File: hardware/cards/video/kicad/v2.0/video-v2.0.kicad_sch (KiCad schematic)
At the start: 108 parts, among them IC1 74ALS08, IC15 IDT7134, IC17 MC6845, IC18 74S85, IC19 74LS00, IC20 74LS04, IC21 74LS90, IC22 74LS175, IC23 74LS174, IC24 74LS166, IC25 2732, IC26 74LS86, IC27 7416, IC28 74LS163, IC30 74LS138, IC31 74LS32, IC32 74LS32, IC33 74LS273, IC34 74LS244, IC35 74LS157, IC36 74LS157, IC37 74LS157, IC38 74LS157, IC39 62256, IC40 74LS244, IC41 74LS374, IC42 74LS374, IC43 74LS166, IC44 74LS74, IC45 74LS20, IC46 74LS04, IC47 74LS08, IC48 74LS10, IC49 ATmega328P-P, IC50 74LS374, IC51 74LS374, IC52 74LS244, IC53 74LS74, J1 RCA, J2 KEYBOARD, J3 MOUSE, J4 FTDI, Q2 12MHz, X1 DIN41612 96, X2 DB9 F, Y1 16MHz

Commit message: feat(video): V2.0 review fixes and two features, board rebuilt
The design review's HIGH and MED fixes in the circuit: V2-1 BUSY/SRC swapped on the ATmega (pins 17/19), V2-2 the
Mini-DIN footprint drawn from the Same Sky MD-60SM data sheet, V2-4 the muxes' select from QC OR RCO, V2-5 IC40 enabled
by -WE, V2-6 MRST through IC27/E,F (D1 gone), V2-7/8 -INT = INTREQ AND FULL (new IC54 74HCT08) with pull-ups on LDDATA
and RDCMD, V2-9/12 HCT parts, V2-10 an AT28C64B-15 character generator; LOW V2-16/17/20/21 (decoupling, PTC, J4
legend, BOM.md).

Direct mode: with GFX-ON = 0 the CPU owns the graphics RAM (NMUX = NAND(QC OR RCO, GFX-ON) holds the CPU address,
-WE = NOT GWR, -OE from the window read, reads through the new bypass buffer IC55 74HCT244, GD pull-ups RN3).
Text-only build: R25/R26 pull-down pads on GDOT and WRQ, IN PC bit 3 = TEXT-ONLY (IC44/B, R27);
text_only_check() proves those are the only nets the left-off parts drive.

build.sh: order 3 complete, 308 vias, DRC 0 unconnected / no copper findings, netlist proof 215/215, ERC off-grid only,
verify PASS (173 key connections). Not to be ordered before the re-review.

Co-Authored-By: Claude Opus 5.5 <noreply@anthropic.com>
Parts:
- removed D1: 1N4148, Diode_THT:D_DO-35_SOD27_P7.62mm_Horizontal, symbol Device:D
- added C58, C59: 100n, Capacitor_THT:C_Disc_D5.0mm_W2.5mm_P2.50mm, symbol Device:C
- added F1: 0.5A PTC, Fuse:Fuse_Bourns_MF-RHT050, symbol Device:Polyfuse
- added IC54: 74HCT08, Package_DIP:DIP-14_W7.62mm, symbol 74xx:74LS08
- added IC55: 74HCT244, Package_DIP:DIP-20_W7.62mm, symbol 74xx:74LS244
- added R21: 4.7k, Resistor_THT:R_Axial_DIN0207_L6.3mm_D2.5mm_P7.62mm_Horizontal, symbol Device:R
- added R22, R23, R24, R27: 10k, Resistor_THT:R_Axial_DIN0207_L6.3mm_D2.5mm_P7.62mm_Horizontal, symbol Device:R
- added R25, R26: 1k, Resistor_THT:R_Axial_DIN0207_L6.3mm_D2.5mm_P7.62mm_Horizontal, symbol Device:R
- added RN3: 10k x8, Resistor_THT:R_Array_SIP9, symbol Device:R_Network08
- C16: value 10u -> 47u; footprint Capacitor_THT:CP_Radial_D5.0mm_P2.50mm -> Capacitor_THT:CP_Radial_D6.3mm_P2.50mm
- IC25: value 2732 -> AT28C64B-15; footprint Package_DIP:DIP-24_W15.24mm -> Package_DIP:DIP-28_W15.24mm; symbol video-v2.0-local:2732 -> Memory_EEPROM:KM28C64A
- IC33: value 74LS273 -> 74HCT273
- IC40: value 74LS244 -> 74HCT244
- IC41, IC51: value 74LS374 -> 74HCT374
- IC53: value 74LS74 -> 74HCT74
- J2, J3: footprint video-v2.0-local:MiniDIN6_PS2 -> video-v2.0-local:MiniDIN6_MD-60SM
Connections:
- net -RESET: now also IC27.11
- net ADDR0: now also IC35.3 (I1a); no longer IC35.2 (I0a)
- net ADDR1: now also IC35.6 (I1b); no longer IC35.5 (I0b)
- net ADDR10: now also IC37.10 (I1c); no longer IC37.11 (I0c)
- net ADDR2: now also IC35.10 (I1c); no longer IC35.11 (I0c)
- net ADDR3: now also IC35.13 (I1d); no longer IC35.14 (I0d)
- net ADDR4: now also IC36.3 (I1a); no longer IC36.2 (I0a)
- net ADDR5: now also IC36.6 (I1b); no longer IC36.5 (I0b)
- net ADDR6: now also IC36.10 (I1c); no longer IC36.11 (I0c)
- net ADDR7: now also IC36.13 (I1d); no longer IC36.14 (I0d)
- net ADDR8: now also IC37.3 (I1a); no longer IC37.2 (I0a)
- net ADDR9: now also IC37.6 (I1b); no longer IC37.5 (I0b)
- net BUSY: now also IC49.17 (PB3); no longer IC49.19 (PB5)
- net CA3: now also IC25.7 (A3); no longer IC25.5 (A3)
- net CA4: now also IC25.6 (A4); no longer IC25.4 (A4)
- net CA5: now also IC25.5 (A5); no longer IC25.3 (A5)
- net CA6: now also IC25.4 (A6); no longer IC25.2 (A6)
- net CA7: now also IC25.3 (A7); no longer IC25.1 (A7)
- net CA8: now also IC25.25 (A8); no longer IC25.23 (A8)
- net CG0: now also IC25.11 (I/O0); no longer IC25.9 (O0)
- net CG1: now also IC25.12 (I/O1); no longer IC25.10 (O1)
- net CG2: now also IC25.13 (I/O2); no longer IC25.11 (O2)
- net CG3: now also IC25.15 (I/O3); no longer IC25.13 (O3)
- net CG4: now also IC25.16 (I/O4); no longer IC25.14 (O4)
- net CG5: now also IC25.17 (I/O5); no longer IC25.15 (O5)
- net CG6: now also IC25.18 (I/O6); no longer IC25.16 (O6)
- net CG7: now also IC25.19 (I/O7); no longer IC25.17 (O7)
- net CPAGE: now also IC38.10 (I1c); no longer IC38.11 (I0c)
- net CRTCCLOCK: now also IC32.9; no longer IC35.1 (S), IC36.1 (S), IC37.1 (S), IC38.1 (S), IC46.1
- net DATA0: now also IC55.18 (O0a)
- net DATA1: now also IC55.16 (O1a)
- net DATA2: now also IC55.14 (O2a)
- net DATA3: now also IC55.12 (O3a)
- net DATA4: now also IC55.9 (O0b)
- net DATA5: now also IC55.7 (O1b)
- net DATA6: now also IC55.5 (O2b)
- net DATA7: now also IC55.3 (O3b)
- net DOTS: now also IC25.21 (A10); no longer IC25.19 (A10)
- net DPAGE: now also IC38.11 (I0c); no longer IC38.10 (I1c)
- net FULL: now also IC54.5
- net GD0: now also IC55.2 (I0a), RN3.2 (R1)
- net GD1: now also IC55.4 (I1a), RN3.3 (R2)
- net GD2: now also IC55.6 (I2a), RN3.4 (R3)
- net GD3: now also IC55.8 (I3a), RN3.5 (R4)
- net GD4: now also IC55.11 (I0b), RN3.6 (R5)
- net GD5: now also IC55.13 (I1b), RN3.7 (R6)
- net GD6: now also IC55.15 (I2b), RN3.8 (R7)
- net GD7: now also IC55.17 (I3b), RN3.9 (R8)
- net GDOT: now also R25.1
- net GFXON: now also IC19.13, IC44.4 (~{S}), IC46.1, IC48.11
- net GND: now also IC25.14 (GND), IC25.2 (A12), IC25.23 (A11), IC25.24 (A9), IC44.13 (~{R}), IC46.13, C58.2, C59.2, IC54.10, IC54.12, IC54.13, IC54.7 (GND), IC54.9, IC55.10 (GND), R24.2, R25.2, R26.2; no longer IC25.12 (GND), IC25.18 (~{CE}), IC25.21 (A11), IC27.11, IC27.13, IC32.10, IC32.12, IC32.13, IC32.9, IC34.8 (I3a)
- net GRDOE: now also IC54.2; no longer IC41.1 (OE)
- net GSEL: now also IC45.9, IC48.9
- net GWE: now also IC40.1 (OEa), IC40.19 (OEb)
- net INTREQ: now also IC54.4, R24.1; no longer IC27.9
- net LDDATA: now also R22.1
- net MEMRD: now also IC45.10, IC48.10
- net MRST: now also IC27.12
- net PLANE0: now also IC37.13 (I1d); no longer IC37.14 (I0d)
- net PLANE1: now also IC38.3 (I1a); no longer IC38.2 (I0a)
- net PLANE2: now also IC38.6 (I1b); no longer IC38.5 (I0b)
- net RCO: now also IC32.10
- net RDCMD: now also R23.1
- net SRC: now also IC49.19 (PB5); no longer IC49.17 (PB3)
- net VADDR0: now also IC35.2 (I0a); no longer IC35.3 (I1a)
- net VADDR1: now also IC35.5 (I0b); no longer IC35.6 (I1b)
- net VADDR10: now also IC37.11 (I0c); no longer IC37.10 (I1c)
- net VADDR2: now also IC35.11 (I0c); no longer IC35.10 (I1c)
- net VADDR3: now also IC35.14 (I0d); no longer IC35.13 (I1d)
- net VADDR4: now also IC36.2 (I0a); no longer IC36.3 (I1a)
- net VADDR5: now also IC36.5 (I0b); no longer IC36.6 (I1b)
- net VADDR6: now also IC36.11 (I0c); no longer IC36.10 (I1c)
- net VADDR7: now also IC36.14 (I0d); no longer IC36.13 (I1d)
- net VADDR8: now also IC37.2 (I0a); no longer IC37.3 (I1a)
- net VADDR9: now also IC37.5 (I0b); no longer IC37.6 (I1b)
- net VCC: now also IC25.27 (~{WE}), IC25.28 (VCC), C58.1, C59.1, F1.1, IC54.14 (VCC), IC55.20 (VCC), R21.2, R22.2, R23.2, R27.2, RN3.1 (common); no longer IC19.12, IC19.13, IC25.24 (VCC), IC44.13 (~{R}), IC44.4 (~{S}), IC45.10, IC45.12, IC45.9, IC48.10, IC48.11, IC48.9, J2.4 (+5V), J3.4 (+5V)
- net VROWS0: now also IC25.10 (A0), IC37.14 (I0d); no longer IC25.8 (A0), IC37.13 (I1d)
- net VROWS1: now also IC25.9 (A1), IC38.2 (I0a); no longer IC25.7 (A1), IC38.3 (I1a)
- net VROWS2: now also IC25.8 (A2), IC38.5 (I0b); no longer IC25.6 (A2), IC38.6 (I1b)
- net WEPH: now also IC32.12; no longer IC45.4
- net WRQ: now also R26.1
- net WSLOT: no longer IC46.13
- net WEPH2: now reaches IC32.11
- net WEPH2: now also IC45.4
- net SRDOE: now reaches IC48.8
- net SRDOE: now also IC41.1 (OE)
- net TXTONLY: now reaches IC44.9 (Q)
- net TXTONLY: now also IC34.8 (I3a), R27.1
- net QCR: now reaches IC32.8
- net QCR: now also IC19.12
- net RESETH: now reaches IC27.10
- net RESETH: now also IC27.13, R21.1
- net DRDOE: now reaches IC45.8
- net DRDOE: now also IC55.1 (OEa), IC55.19 (OEb)
- net NMUX: now reaches IC19.11
- net NMUX: now also IC35.1 (S), IC36.1 (S), IC37.1 (S), IC38.1 (S), IC45.2, IC54.1
- removed net -WSLOT: IC40.1 (OEa), IC40.19 (OEb), IC46.12
- removed net NQC: IC1.5, IC45.2, IC46.2
- new net INTG: IC27.9, IC54.6
- new net NGFX: IC32.13, IC45.12, IC46.2
- new net OEY: IC1.5, IC54.3
- new net PS2VCC: F1.2, J2.4 (+5V), J3.4 (+5V)
- no-connect marks 91 -> 88
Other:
- note added: "GRAPHICS RAM $D800-$DFFF: SLOT LOGIC (GFX-ON = 1) / DIRECT MODE (GFX-ON = 0)"
- note removed: "GRAPHICS RAM $D800-$DFFF: SLOT LOGIC (QC: CPU / DISPLAY HALF)"
- moved on the sheet: C16, C17, C18, C19, C20, C21, C22, C23, C24, C25, C26, C27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

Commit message: fix(video): V2.0 rebuilt for the re-review - R2-1 Mini-DIN side-leg slots 1.2 x 2.6, R2-2 IC55 up 0.6 mm, R2-3 -RESET buffered by IC54/C
R2-1: MD-60SM side-leg slots 2.6 x 1.2 mm plated, pads 3.3 x 1.9, same centres (the 0.54 mm legs now 0.21 mm inside
the outer wall, 0.45 inside the inner; earth slot unchanged). R2-2: IC55 at (156.0, 78.7): 3.30 mm from IC19/IC1's end
pins, 3.22 from IC42's (a socket needs <= 3.2). R2-3: IC27/E's input is RESETB = IC54/C (74HCT08, -RESET AND VCC: a
buffer, same sense), so the bus -RESET sees one HCT input. R2-14: verify's KEY +16 nets (MEMWR path, IC44.1, IC53/A,
IC40 A/Y, the jacks' shields), check() fails on a left-off IC without an OUTPUTS entry.
Routed anew: order 6 (orders 3, 4, 17, 0, 1, 2, 5, 7 tried; 5 also clean): 0 unrouted, 328 vias. Netlist proof MATCH
216/216, DRC 0 unconnected / no copper findings / parity 0, ERC off-grid only, verify PASS (189).

Co-Authored-By: Claude Opus 5.5 <noreply@anthropic.com>
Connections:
- net -RESET: now also IC54.9; no longer IC27.11
- net GND: no longer IC54.10, IC54.9
- net VCC: now also IC54.10
- net RESETB: now reaches IC54.8
- net RESETB: now also IC27.11
- no-connect marks 88 -> 87
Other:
- moved on the sheet: IC54C, IC54D

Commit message: fix(video): V2.0 rebuilt for the rest of the re-review - socket-outline check (R2-2), the 6845's B grade and C16 16 V (R2-7), the silkscreen placed clear (R2-9)
R2-2: gen_v20.py place now checks every DIP socket's outline (pin rows + 1.3 mm at the sides, end pins + 1.9 mm at
the ends: the widest stamped sockets) against every other socket and every part's pads and body, over the whole
board (socket_check). It found RN3 and C59 meeting IC55's end wall: both 0.3 mm left. PASS, the closest IC42 / IC55
0.02 mm, IC19 / IC1 / IC55 0.10.
R2-7: IC17's value HD68B45SP / MC68B45P (the 2 MHz bus grade; Hitachi's letters to verify on the part), C16 47u 16V;
BUY notes for IC39 (-55 recommended, R2-8), IC41 / IC55 (74ACT fallback, R2-6), C16; BOM.md regenerated.
R2-9: silk_place() puts every reference and legend clear of the other silk, the pads, the edge and other parts'
bodies; the jack legends turned beside the jacks; the MD-60SM outline broken round its side-leg pads and short of
the edge; X2's "F09" to Fab, X1's small texts to 0.8 / 0.12 mm. DRC silk_overlap 40 -> 0, silk_over_copper 89 -> 8
(J1 / X2 library outlines), silk_edge_clearance 10 -> 8, text height / thickness 5 -> 0.
Routed anew: order 5 (orders 6 and 5 complete, 4 left 2): 0 unrouted, 285 vias, 22.1 m. A repeat of order 5 did not
reproduce it (2 unrouted), so the board is that run's route with silk_place() re-applied (texts only) and build.sh's
reports and checks run on it: netlist proof MATCH 216/216, DRC 0 unconnected / no copper findings / parity 0, ERC
off-grid only, planes one piece each, verify PASS (189), text-only check PASS. build.sh's default order is 5.

Co-Authored-By: Claude Opus 5.5 <noreply@anthropic.com>
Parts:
- C16: value 47u -> 47u 16V
- IC17: value MC6845 -> HD68B45SP / MC68B45P
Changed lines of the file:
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@@
 	(title_block
 		(title "YACC1 video card V2.0")
-		(date "2026-10-22")
+		(date "2026-10-23")
 		(rev "V2.0")
 		(company "YACC1")
@@
 			)
 		)
-		(property "Value" "47u"
+		(property "Value" "47u 16V"
 			(at 854.075 154.94 0)
 			(show_name no)
@@
 			)
 		)
-		(property "Value" "MC6845"
+		(property "Value" "HD68B45SP / MC68B45P"
 			(at 474.98 52.07 0)
 			(show_name no)
@@
 		(pin "3"
 		)
-		(pin "4"
-		)
-		(pin "5"
-		)
 		(pin "6"
 		)
@@
 		(pin "14"
 		)
+		(pin "4"
+		)
+		(pin "5"
+		)
 		(instances
 			(project "video-v2.0"
@@
 		(pin "6"
 		)
-		(pin "1"
-		)
-		(pin "2"
-		)
-		(pin "3"
-		)
 		(pin "8"
 		)
@@
 		(pin "14"
 		)
+		(pin "1"
+		)
+		(pin "2"
+		)
+		(pin "3"
+		)
 		(instances

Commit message: feat(video): V2.0 schematic drawn by function - a root and eight wired sheets
gen_v20.py sch draws the schematic with tools/kicad/sch_wire.py: one sheet per
block (bus and ports, CRTC, text, clocks, graphics, video out, PS/2, power),
the parts placed by ELK and 153 nets drawn as wires (before: one A0 sheet, 669
label stubs, no pin wired to another). Every sub-sheet net reaches the root as
a sheet pin with a local label, so KiCad names it /NAME exactly as the board and
its Gerbers do; a net drawn on one sheet only has a pin on both sides of its
sheet symbol (KiCad's ERC needs a second root label to count one connected).

Schematic only - no Freerouting, no build.sh. The board file changes only in
its footprints' (path ...) lines (gen_v20.py link: 105 now carry the sheet
UUID, the 15 multi-unit parts got the link they lacked). Proofs: checknet MATCH
216 nets; compare_netlists MATCH 216/216; all 1034 pad net names identical;
verify PASS (189); DRC 0 unconnected, schematic parity 0; ERC 0 errors, 0
warnings (before: 6 endpoint_off_grid warnings); Gerbers re-exported with the
README's Ordering commands into a scratch folder equal gerbers/ apart from
their timestamp lines. .kicad_pro: the sheet list.

Co-Authored-By: Claude Opus 5.5 <noreply@anthropic.com>
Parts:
- removed C16: 47u 16V, Capacitor_THT:CP_Radial_D6.3mm_P2.50mm, symbol Device:C_Polarized
- removed C17, C18, C19, C20, C21, C22, C23, C24, C25, C26, C27, C28, C29, C3, C30, C31, C32, C33, C34, C35, C36, C37, C38, C39, C40, C41, C42, C43, C44, C45, C46, C47, C48, C49, C50, C51, C52, C53, C54, C57, C58, C59: 100n, Capacitor_THT:C_Disc_D5.0mm_W2.5mm_P2.50mm, symbol Device:C
- removed C55, C56: 22p, Capacitor_THT:C_Disc_D5.0mm_W2.5mm_P2.50mm, symbol Device:C
- removed F1: 0.5A PTC, Fuse:Fuse_Bourns_MF-RHT050, symbol Device:Polyfuse
- removed IC1: 74ALS08, Package_DIP:DIP-14_W7.62mm, symbol 74xx:74LS08
- removed IC15: IDT7134, Package_DIP:DIP-48_W15.24mm, symbol video-v2.0-local:IDT7134
- removed IC17: HD68B45SP / MC68B45P, Package_DIP:DIP-40_W15.24mm, symbol GPU:MC6845
- removed IC18: 74S85, Package_DIP:DIP-16_W7.62mm, symbol 74xx:74LS85
- removed IC19: 74LS00, Package_DIP:DIP-14_W7.62mm, symbol 74xx:74LS00
- removed IC20, IC46: 74LS04, Package_DIP:DIP-14_W7.62mm, symbol 74xx:74LS04
- removed IC21: 74LS90, Package_DIP:DIP-14_W7.62mm, symbol 74xx:74LS90
- removed IC22: 74LS175, Package_DIP:DIP-16_W7.62mm, symbol 74xx:74LS175
- removed IC23: 74LS174, Package_DIP:DIP-16_W7.62mm, symbol 74xx:74LS174
- removed IC24, IC43: 74LS166, Package_DIP:DIP-16_W7.62mm, symbol 74xx:74LS166
- removed IC25: AT28C64B-15, Package_DIP:DIP-28_W15.24mm, symbol Memory_EEPROM:KM28C64A
- removed IC26: 74LS86, Package_DIP:DIP-14_W7.62mm, symbol 74xx:74LS86
- removed IC27: 7416, Package_DIP:DIP-14_W7.62mm, symbol 74xx:74LS05
- removed IC28: 74LS163, Package_DIP:DIP-16_W7.62mm, symbol 74xx:74LS161
- removed IC30: 74LS138, Package_DIP:DIP-16_W7.62mm, symbol 74xx:74LS138
- removed IC31, IC32: 74LS32, Package_DIP:DIP-14_W7.62mm, symbol 74xx:74LS32
- removed IC33: 74HCT273, Package_DIP:DIP-20_W7.62mm, symbol 74xx:74LS273
- removed IC34, IC52: 74LS244, Package_DIP:DIP-20_W7.62mm, symbol 74xx:74LS244
- removed IC35, IC36, IC37, IC38: 74LS157, Package_DIP:DIP-16_W7.62mm, symbol 74xx:74LS157
- removed IC39: 62256, Package_DIP:DIP-28_W15.24mm, symbol Memory_RAM:KM62256CLP
- removed IC40, IC55: 74HCT244, Package_DIP:DIP-20_W7.62mm, symbol 74xx:74LS244
- removed IC41, IC51: 74HCT374, Package_DIP:DIP-20_W7.62mm, symbol 74xx:74LS374
- removed IC42, IC50: 74LS374, Package_DIP:DIP-20_W7.62mm, symbol 74xx:74LS374
- removed IC44: 74LS74, Package_DIP:DIP-14_W7.62mm, symbol 74xx:74LS74
- removed IC45: 74LS20, Package_DIP:DIP-14_W7.62mm, symbol 74xx:74LS20
- removed IC47: 74LS08, Package_DIP:DIP-14_W7.62mm, symbol 74xx:74LS08
- removed IC48: 74LS10, Package_DIP:DIP-14_W7.62mm, symbol 74xx:74LS10
- removed IC49: ATmega328P-P, Package_DIP:DIP-28_W7.62mm, symbol MCU_Microchip_ATmega:ATmega48PV-10P
- removed IC53: 74HCT74, Package_DIP:DIP-14_W7.62mm, symbol 74xx:74LS74
- removed IC54: 74HCT08, Package_DIP:DIP-14_W7.62mm, symbol 74xx:74LS08
- removed J1: RCA, video-v2.0-local:RCA, symbol video-v2.0-local:RCA
- removed J2: KEYBOARD, video-v2.0-local:MiniDIN6_MD-60SM, symbol video-v2.0-local:MINIDIN6
- removed J3: MOUSE, video-v2.0-local:MiniDIN6_MD-60SM, symbol video-v2.0-local:MINIDIN6
- removed J4: FTDI, Connector_PinHeader_2.54mm:PinHeader_1x06_P2.54mm_Vertical, symbol Connector_Generic:Conn_01x06
- removed JP2: DOTS 8=ON, Connector_PinHeader_2.54mm:PinHeader_1x02_P2.54mm_Vertical, symbol Connector_Generic:Conn_01x02
- removed JP3: INT-EN, Connector_PinHeader_2.54mm:PinHeader_1x02_P2.54mm_Vertical, symbol Connector_Generic:Conn_01x02
- removed LED1: PWR, LED_THT:LED_D5.0mm, symbol Device:LED
- removed Q2: 12MHz, Crystal:Crystal_HC49-U_Vertical, symbol Device:Crystal
- removed R10, R25, R26, R8, R9: 1k, Resistor_THT:R_Axial_DIN0207_L6.3mm_D2.5mm_P7.62mm_Horizontal, symbol Device:R
- removed R11: 33, Resistor_THT:R_Axial_DIN0207_L6.3mm_D2.5mm_P7.62mm_Horizontal, symbol Device:R
- removed R12: 270, Resistor_THT:R_Axial_DIN0207_L6.3mm_D2.5mm_P7.62mm_Horizontal, symbol Device:R
- removed R15, R17, R18, R19, R20, R21: 4.7k, Resistor_THT:R_Axial_DIN0207_L6.3mm_D2.5mm_P7.62mm_Horizontal, symbol Device:R
- removed R16, R22, R23, R24, R27: 10k, Resistor_THT:R_Axial_DIN0207_L6.3mm_D2.5mm_P7.62mm_Horizontal, symbol Device:R
- removed R2: 330, Resistor_THT:R_Axial_DIN0207_L6.3mm_D2.5mm_P10.16mm_Horizontal, symbol Device:R
- removed RN2: 10k x4, Resistor_THT:R_Array_SIP5, symbol Device:R_Network04
- removed RN3: 10k x8, Resistor_THT:R_Array_SIP9, symbol Device:R_Network08
- removed SV3: BLOCK, Connector_PinHeader_2.54mm:PinHeader_2x04_P2.54mm_Vertical, symbol Connector_Generic:Conn_02x04_Odd_Even
- removed SV4: DOTCLK, Connector_PinHeader_2.54mm:PinHeader_1x03_P2.54mm_Vertical, symbol Connector_Generic:Conn_01x03
- removed X1: DIN41612 96, blank-card-v3.2-eagle:FABC96R, symbol blank-card-v3.2-eagle:FABC96R
- removed X2: DB9 F, video-v2.0-local:F09HP, symbol video-v2.0-local:DE9_SHIELD
- removed Y1: 16MHz, Crystal:Crystal_HC49-U_Vertical, symbol Device:Crystal
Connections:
- no-connect marks 87 -> 0
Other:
- added sheet Bus and ports (video-v2.0-bus.kicad_sch)
- added sheet CRTC (video-v2.0-crtc.kicad_sch)
- added sheet Clocks (video-v2.0-clock.kicad_sch)
- added sheet Graphics (video-v2.0-gfx.kicad_sch)
- added sheet PS2 (video-v2.0-ps2.kicad_sch)
- added sheet Power (video-v2.0-power.kicad_sch)
- added sheet Text (video-v2.0-text.kicad_sch)
- added sheet Video out (video-v2.0-video.kicad_sch)
- note added: "The video card V2.0, one sheet per functional block: sheet 2 Bus and ports BUS INTERFACE, PORT DECODE, CONTROL AND STATUS (PA-PE) sheet 3 CRTC 6845 CRTC ON PORTS PA (ADDRESS) / PB (DATA) sheet 4 Text BOARD SELECT ($D000 BLOCK), TEXT RAM $D000-$D7FF, CHARACTER GENERATOR, TEXT DOT SHIFTER sheet 5 Clocks DOT CLOCK, CHARACTER COUNTER (DOTS: 6 OR 8 DOTS A CHARACTER) sheet 6 Graphics GRAPHICS RAM $D800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"
- note removed: "BOARD SELECT ($D000 BLOCK) + TEXT RAM $D000-$D7FF"
- note removed: "BUS X1 DIN 41612 (YACC1 V3.2)"
- note removed: "CLOCKS + CHARACTER PIPELINE (DOTS: 6 OR 8 DOTS A CHARACTER)"
- note removed: "DOT COMBINE + VIDEO OUT"
- note removed: "GRAPHICS RAM $D800-$DFFF: SLOT LOGIC (GFX-ON = 1) / DIRECT MODE (GFX-ON = 0)"
- note removed: "PORTS PA-PE: 6845 (PA/PB), CONTROL + STATUS (PC)"
- note removed: "POWER UNITS + DECOUPLING"
- note removed: "PS/2: ATMEGA328P + LATCHES (PD, PE), INT"
- note removed: "PWR_FLAGs: the bus supplies VCC and GND (X1, six pins each)."

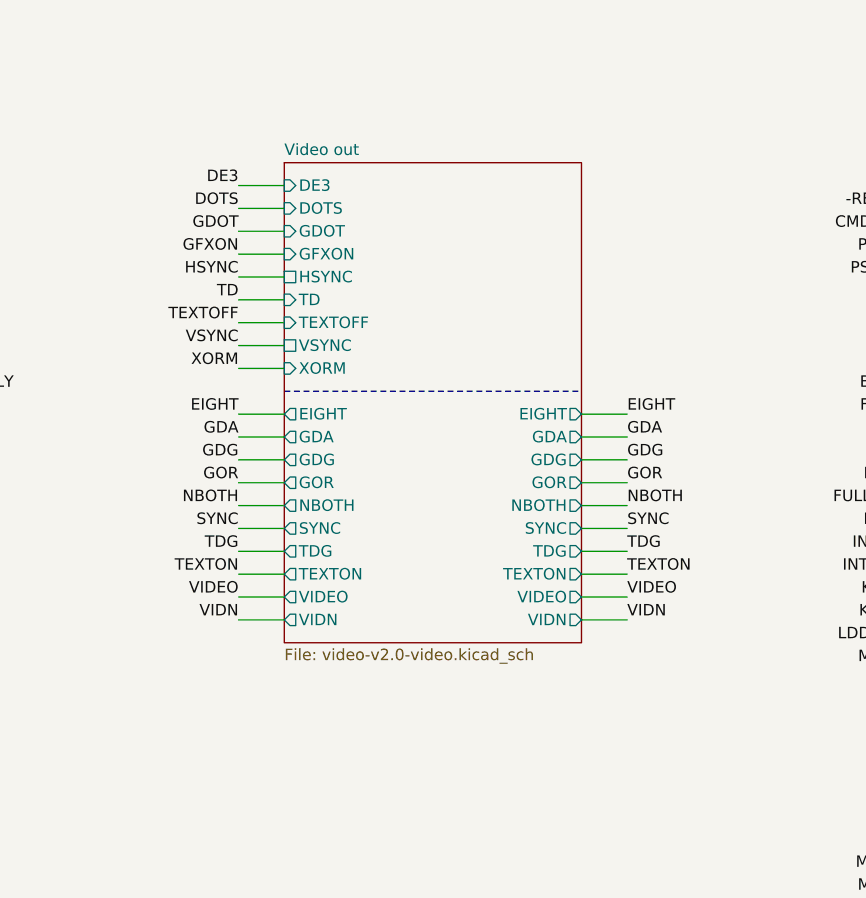
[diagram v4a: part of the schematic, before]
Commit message: feat(video): V2.0 DB9 VSYNC polarity jumper JP4, board routed afresh
DB9 pin 9 now carries the 6845's VSYNC buffered by IC54/D (JP4 1-2,
+VSYNC: TV rate, IBM 5153 CGA) or inverted by IC46/F (JP4 2-3, -VSYNC:
IBM 5151 MDA); DB9 pin 2 joins pin 1 on GND. IC46/F and IC54/D were the
spare gates; IC38's fourth section is the only spare left. 121 parts,
219 nets. JP4 stands beside the DB9 with "+VS CGA" / "-VS MDA" on the silk.

The old copper could not take the change (IC46/F walled in by row A's
tracks), so build.sh routed the board from scratch: order 3 of 1, 2, 3,
7 kept, 0 unrouted, 314 vias, 22.9 m. Netlist proof MATCH 219/219, DRC 0
unconnected and no copper findings (cosmetic silk items as before),
verify PASS with 204 key connections, planes one piece each, sockets
PASS. Gerbers and zip exported again 2026-10-27; BOM, README, order
notes, BACKLOG updated; review r3 notes the board changed after it.
Not ordered.

Co-Authored-By: Claude Opus 5.5 <noreply@anthropic.com>
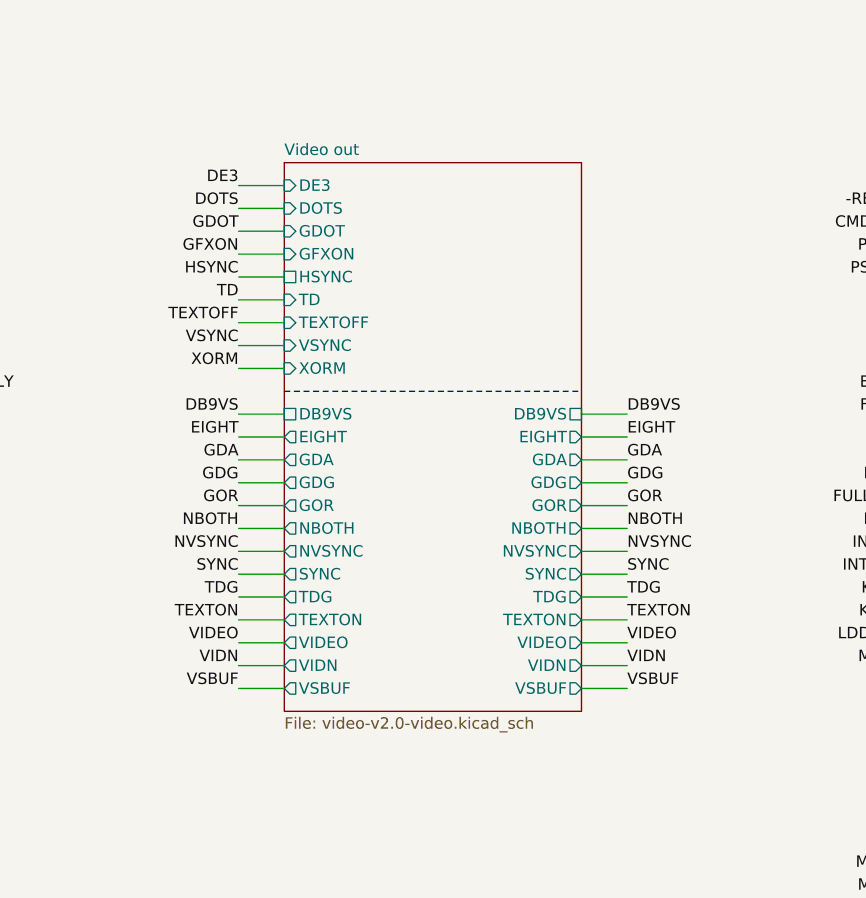
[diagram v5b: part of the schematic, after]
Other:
- sheet Video out ports: added DB9VS, NVSYNC, VSBUF; removed none
